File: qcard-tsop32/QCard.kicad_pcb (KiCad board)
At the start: 2 copper layers, 55 x 32 mm, 6 parts, among them J1 Conn_02x18_Top_Bottom, U1 SST39SF040

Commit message: update date
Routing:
- net /GND: vias 3 -> 2
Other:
- board size 55 x 32 mm -> 55 x 31.5 mm
- board text added: "PROGRAM"
- board text added: "READ"
- board text removed: "1"
- board text removed: "18"
- board text removed: "19"
- board text removed: "36"
- board text removed: "PROGRAM / PIN 18"
- board text removed: "READ / VIH"
- board text removed: "WE#"
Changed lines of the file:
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@@
   (title_block
     (title "Q-Card 4Mbit Flash")
-    (date "2023-01-24")
+    (date "2023-01-18")
     (rev "1903842")
     (company "@partlyhuman")
@@
     (property "Sheetname" "")
     (attr through_hole)
-    (fp_text reference "U1" (at 0 -5.4525) (layer "F.Fab")
+    (fp_text reference "U1" (at 0 -5.4525) (layer "F.SilkS")
       (effects (font (size 1 1) (thickness 0.15)))
     )
@@
     )
   )
-  (gr_line (start 105 84.25) (end 105 63) (layer "Edge.Cuts") (width 0.1))
-  (gr_line (start 50 63) (end 50 84.25) (layer "Edge.Cuts") (width 0.1))
+  (gr_line (start 105 84.25) (end 105 63.5) (layer "Edge.Cuts") (width 0.1))
+  (gr_line (start 50 63.5) (end 50 84.25) (layer "Edge.Cuts") (width 0.1))
   (gr_arc (start 54.5 95) (mid 53.792893 94.707107) (end 53.5 94) (layer "Edge.Cuts") (width 0.1))
   (gr_arc (start 101.5 94) (mid 101.207107 94.707107) (end 100.5 95) (layer "Edge.Cuts") (width 0.1))
@@
   (gr_line (start 100.5 95) (end 54.5 95) (layer "Edge.Cuts") (width 0.1))
   (gr_line (start 50 84.25) (end 53.5 84.25) (layer "Edge.Cuts") (width 0.1))
-  (gr_line (start 50 63) (end 105 63) (layer "Edge.Cuts") (width 0.1))
+  (gr_line (start 50 63.5) (end 105 63.5) (layer "Edge.Cuts") (width 0.1))
   (gr_line (start 53.5 84.25) (end 53.5 94) (layer "Edge.Cuts") (width 0.1))
   (gr_line (start 101.5 94) (end 101.5 84.25) (layer "Edge.Cuts") (width 0.1))
   (gr_line (start 77.5 50) (end 77.5 95) (layer "User.1") (width 0.15))
-  (gr_text "36" (at 99 83) (layer "B.SilkS")
-    (effects (font (size 0.5 0.5) (thickness 0.1)) (justify mirror))
-  )
-  (gr_text "19" (at 56 83) (layer "B.SilkS")
-    (effects (font (size 0.5 0.5) (thickness 0.1)) (justify mirror))
-  )
-  (gr_text "READ / VIH" (at 62.5 70.2) (layer "F.SilkS")
+  (gr_text "Q-Chord song cartridge 4Mbit\n${COMPANY} ${ISSUE_DATE}" (at 77.5 67.5) (layer "B.SilkS")
+    (effects (font (size 1.25 1.25) (thickness 0.15)) (justify mirror))
+  )
+  (gr_text "READ" (at 62.5 70.2) (layer "F.SilkS")
     (effects (font (size 0.5 0.5) (thickness 0.1)))
   )
-  (gr_text "PROGRAM / PIN 18" (at 62.5 64.75) (layer "F.SilkS")
-    (effects (font (size 0.5 0.5) (thickness 0.1)))
-  )
-  (gr_text "Q-Chord song cartridge 4Mbit\n${COMPANY} ${ISSUE_DATE}" (at 77.5 79.5) (layer "F.SilkS")
-    (effects (font (size 1.25 1.25) (thickness 0.15)))
-  )
-  (gr_text "WE#" (at 64 67.5) (layer "F.SilkS")
-    (effects (font (size 0.5 0.5) (thickness 0.1)) (justify left))
-  )
-  (gr_text "1" (at 56 83) (layer "F.SilkS")
-    (effects (font (size 0.5 0.5) (thickness 0.1)))
-  )
-  (gr_text "18" (at 99 83) (layer "F.SilkS")
+  (gr_text "PROGRAM" (at 62.5 65) (layer "F.SilkS")
     (effects (font (size 0.5 0.5) (thickness 0.1)))
   )
@@
   (via (at 90 69.75) (size 0.9) (drill 0.4) (layers "F.Cu" "B.Cu") (net 2))
   (via (at 56.3 73.5) (size 0.8) (drill 0.4) (layers "F.Cu" "B.Cu") (free) (net 2))
-  (via (at 100.5 73.5) (size 0.8) (drill 0.4) (layers "F.Cu" "B.Cu") (free) (net 2))
   (segment (start 60.99 89) (end 60.99 78.01) (width 0.25) (layer "F.Cu") (net 3))
   (segment (start 69.297499 69.702501) (end 72.201377 69.702501) (width 0.25) (layer "F.Cu") (net 3))
@@
         (xy 105 84.25)
         (xy 50 84.25)
-        (xy 50 63)
-        (xy 105 63)
+        (xy 50 50)
+        (xy 105 50)
       )
     )

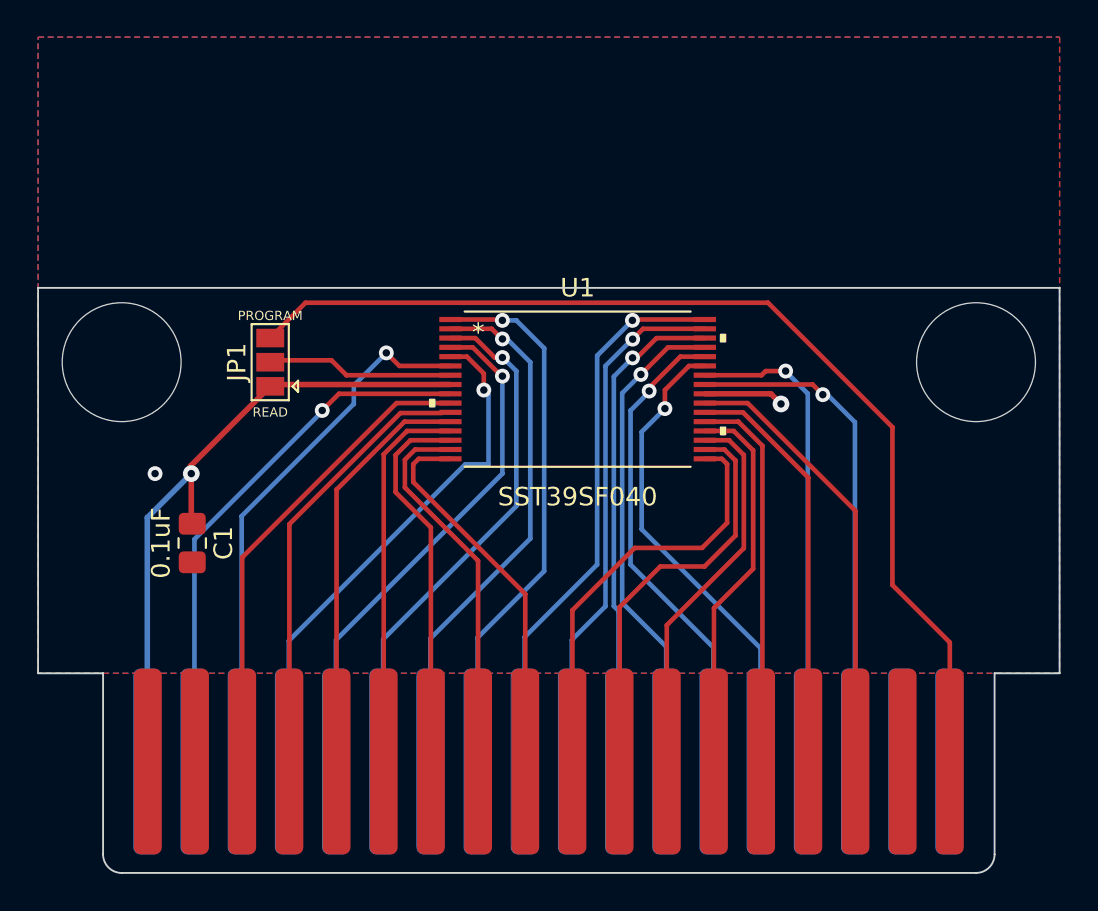
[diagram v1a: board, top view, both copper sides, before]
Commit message: Extra grounding and better silkscreen positioning on smaller pcb
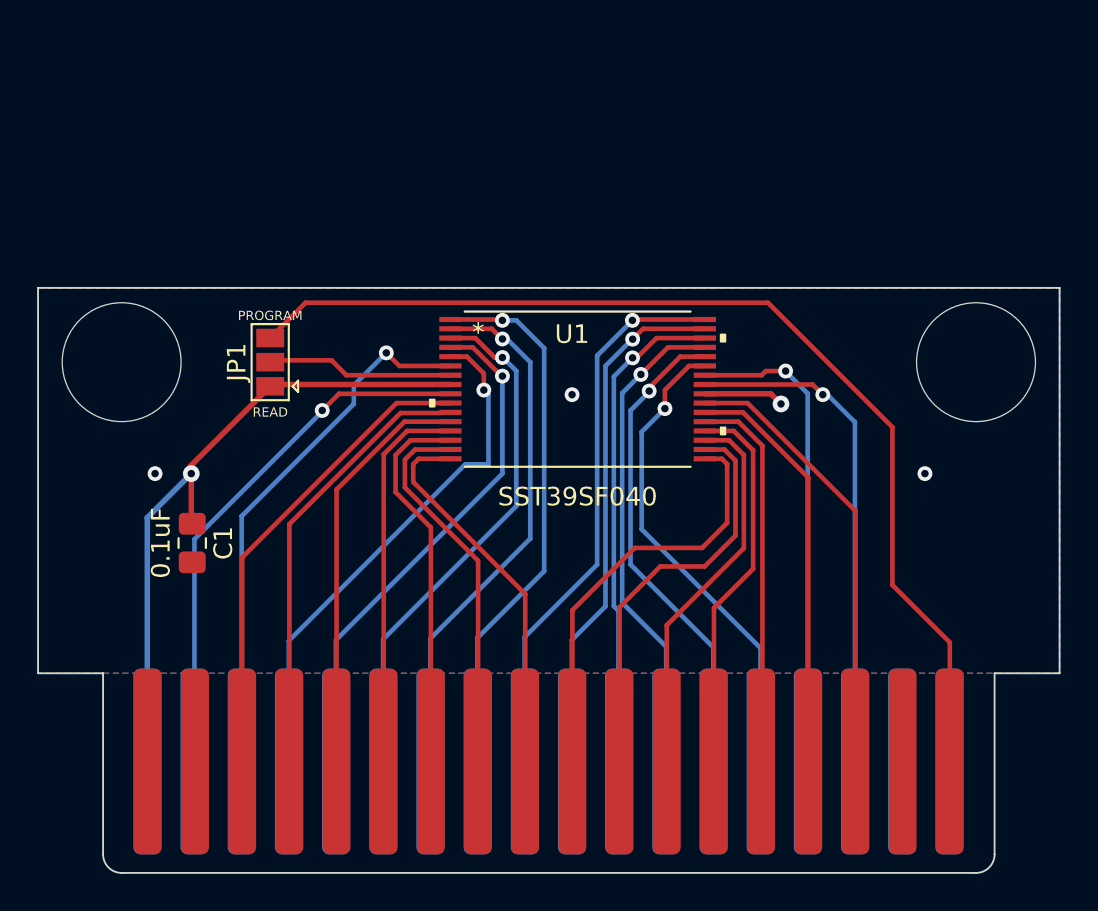
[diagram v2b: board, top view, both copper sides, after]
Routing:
- net /GND: vias 2 -> 4
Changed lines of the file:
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@@
   (title_block
     (title "Q-Card 4Mbit Flash")
-    (date "2023-01-18")
+    (date "2023-01-26")
     (rev "1903842")
     (company "@partlyhuman")
@@
     (property "Sheetname" "")
     (attr through_hole)
-    (fp_text reference "U1" (at 0 -5.4525) (layer "F.SilkS")
+    (fp_text reference "U1" (at -0.300225 -2.9525) (layer "F.SilkS")
       (effects (font (size 1 1) (thickness 0.15)))
     )
@@
   (gr_line (start 101.5 94) (end 101.5 84.25) (layer "Edge.Cuts") (width 0.1))
   (gr_line (start 77.5 50) (end 77.5 95) (layer "User.1") (width 0.15))
-  (gr_text "Q-Chord song cartridge 4Mbit\n${COMPANY} ${ISSUE_DATE}" (at 77.5 67.5) (layer "B.SilkS")
+  (gr_text "Q-Chord song cartridge 4Mbit\n${COMPANY} ${ISSUE_DATE}" (at 77.5 76) (layer "B.SilkS")
     (effects (font (size 1.25 1.25) (thickness 0.15)) (justify mirror))
   )
@@
   (segment (start 85.899073 69.2025) (end 89.4525 69.2025) (width 0.3) (layer "F.Cu") (net 2))
   (segment (start 89.4525 69.2025) (end 90 69.75) (width 0.3) (layer "F.Cu") (net 2))
+  (via (at 78.75 69.25) (size 0.8) (drill 0.4) (layers "F.Cu" "B.Cu") (free) (net 2))
+  (via (at 97.75 73.5) (size 0.8) (drill 0.4) (layers "F.Cu" "B.Cu") (free) (net 2))
   (via (at 90 69.75) (size 0.9) (drill 0.4) (layers "F.Cu" "B.Cu") (net 2))
   (via (at 56.3 73.5) (size 0.8) (drill 0.4) (layers "F.Cu" "B.Cu") (free) (net 2))
@@
         (xy 105 84.25)
         (xy 50 84.25)
-        (xy 50 50)
-        (xy 105 50)
+        (xy 50 63.5)
+        (xy 105 63.5)
       )
     )
